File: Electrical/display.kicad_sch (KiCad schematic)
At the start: 22 parts, among them J4 Conn_02x04_Top_Bottom, U11 JM-S05422A-001, U6 DA56-11CGKWA

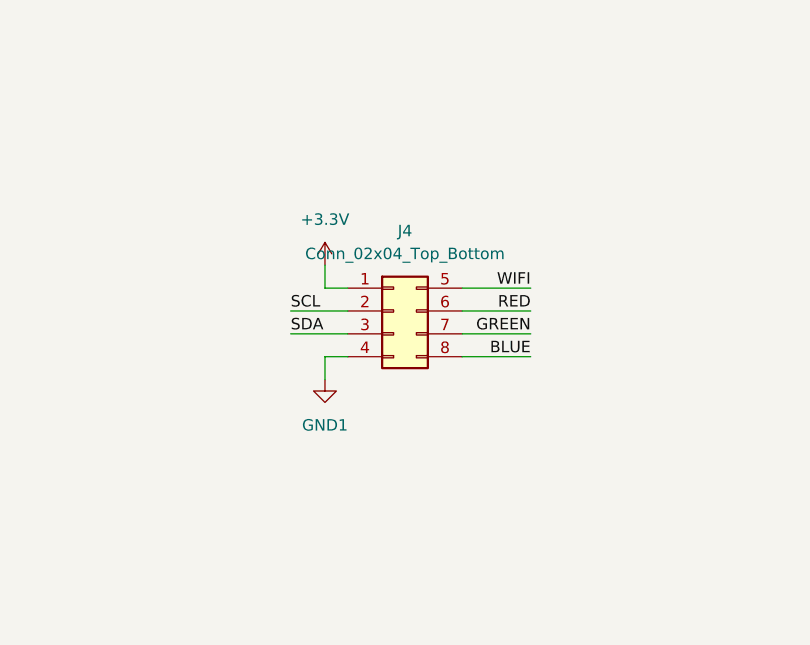
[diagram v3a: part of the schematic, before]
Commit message: Updated Display
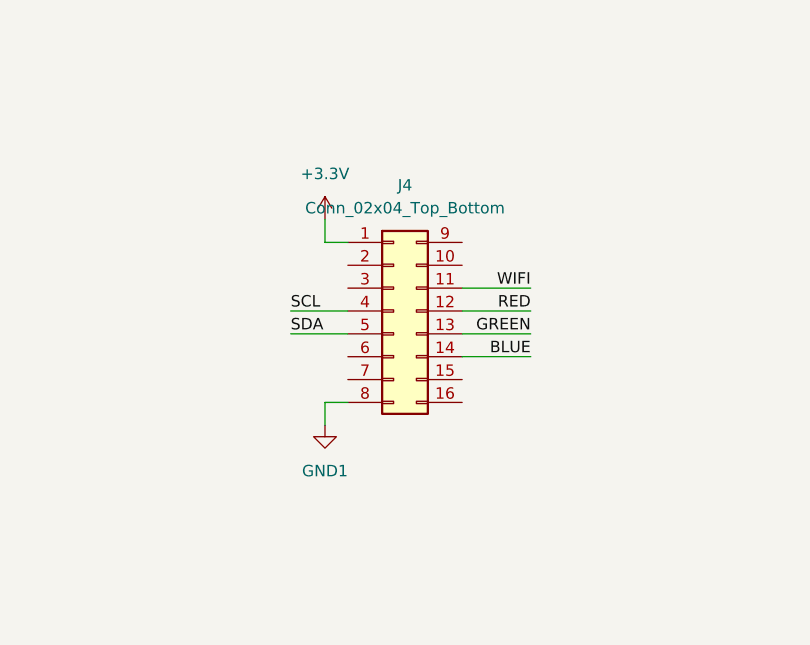
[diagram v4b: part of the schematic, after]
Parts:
- J4: footprint Connector_IDC:IDC-Header_2x04_P2.54mm_Vertical -> Connector_IDC:IDC-Header_2x08_P2.54mm_Vertical; symbol Connector_Generic:Conn_02x04_Top_Bottom -> Connector_Generic:Conn_02x08_Top_Bottom
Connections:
- net BLUE: now also J4.14 (Pin_14); no longer J4.8 (Pin_8)
- net GND1: now also J4.8 (Pin_8); no longer J4.4 (Pin_4)
- net GREEN: now also J4.13 (Pin_13); no longer J4.7 (Pin_7)
- net RED: now also J4.12 (Pin_12); no longer J4.6 (Pin_6)
- net SCL: now also J4.4 (Pin_4); no longer J4.2 (Pin_2)
- net SDA: now also J4.5 (Pin_5); no longer J4.3 (Pin_3)
- net WIFI: now also J4.11 (Pin_11); no longer J4.5 (Pin_5)
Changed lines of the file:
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@@
+    (stroke (width 0) (type default))
+  )
+  (wire (pts (xy 251.46 87.63) (xy 254 87.63))
     (stroke (width 0) (type default))
   )
@@
     (stroke (width 0) (type default))
   )
-  (wire (pts (xy 254 100.33) (xy 251.46 100.33))
+  (wire (pts (xy 251.46 85.09) (xy 251.46 87.63))
     (stroke (width 0) (type default))
   )
@@
     (stroke (width 0) (type default))
   )
-  (wire (pts (xy 251.46 100.33) (xy 251.46 102.87))
+  (wire (pts (xy 251.46 105.41) (xy 251.46 107.95))
     (stroke (width 0) (type default))
   )
@@
     (stroke (width 0) (type default))
   )
+  (wire (pts (xy 254 105.41) (xy 251.46 105.41))
+    (stroke (width 0) (type default))
+  )
   (wire (pts (xy 328.93 184.15) (xy 256.54 184.15))
     (stroke (width 0) (type default))
@@
     (stroke (width 0) (type default))
   )
-  (wire (pts (xy 251.46 90.17) (xy 251.46 92.71))
-    (stroke (width 0) (type default))
-  )
   (wire (pts (xy 140.97 20.32) (xy 140.97 85.09))
     (stroke (width 0) (type default))
@@
   )
   (wire (pts (xy 323.85 167.64) (xy 321.31 167.64))
-    (stroke (width 0) (type default))
-  )
-  (wire (pts (xy 251.46 92.71) (xy 254 92.71))
     (stroke (width 0) (type default))
   )
@@
     )
   )
-  (symbol (lib_id "power:GND1") (at 251.46 102.87 0) (unit 1)
-    (in_bom yes) (on_board yes) (dnp no) (fields_autoplaced)
-    (property "Reference" "#PWR024" (at 251.46 109.22 0)
-      (effects (font (size 1.27 1.27)) hide)
-    )
-    (property "Value" "GND1" (at 251.46 107.95 0)
-      (effects (font (size 1.27 1.27)))
-    )
-    (property "Footprint" "" (at 251.46 102.87 0)
-      (effects (font (size 1.27 1.27)) hide)
-    )
-    (property "Datasheet" "" (at 251.46 102.87 0)
-      (effects (font (size 1.27 1.27)) hide)
-    )
-    (pin "1")
-    (instances
-      (project "NMEA-2000-influxdb"
-        (path "/efe7a42c-525a-4afc-8476-4cc785240ca6/f595a6b6-5945-4ca8-806c-a50feeda2cc9"
-          (reference "#PWR024") (unit 1)
-        )
-      )
-    )
-  )
   (symbol (lib_id "power:+3.3V") (at 346.71 30.48 0) (unit 1)
     (in_bom yes) (on_board yes) (dnp no) (fields_autoplaced)
@@
     )
   )
+  (symbol (lib_id "power:+3.3V") (at 251.46 85.09 0) (unit 1)
+    (in_bom yes) (on_board yes) (dnp no) (fields_autoplaced)
+    (property "Reference" "#PWR023" (at 251.46 88.9 0)
+      (effects (font (size 1.27 1.27)) hide)
+    )
+    (property "Value" "+3.3V" (at 251.46 80.01 0)
+      (effects (font (size 1.27 1.27)))
+    )
+    (property "Footprint" "" (at 251.46 85.09 0)
+      (effects (font (size 1.27 1.27)) hide)
+    )
+    (property "Datasheet" "" (at 251.46 85.09 0)
+      (effects (font (size 1.27 1.27)) hide)
+    )
+    (pin "1")
+    (instances
+      (project "NMEA-2000-influxdb"
+        (path "/efe7a42c-525a-4afc-8476-4cc785240ca6/f595a6b6-5945-4ca8-806c-a50feeda2cc9"
+          (reference "#PWR023") (unit 1)
+        )
+      )
+    )
+  )
   (symbol (lib_id "Device:R") (at 270.51 212.09 90) (mirror x) (unit 1)
     (in_bom yes) (on_board yes) (dnp no)
@@
     )
   )
-  (symbol (lib_id "power:+3.3V") (at 251.46 90.17 0) (unit 1)
-    (in_bom yes) (on_board yes) (dnp no) (fields_autoplaced)
-    (property "Reference" "#PWR023" (at 251.46 93.98 0)
-      (effects (font (size 1.27 1.27)) hide)
-    )
-    (property "Value" "+3.3V" (at 251.46 85.09 0)
-      (effects (font (size 1.27 1.27)))
-    )
-    (property "Footprint" "" (at 251.46 90.17 0)
-      (effects (font (size 1.27 1.27)) hide)
-    )
-    (property "Datasheet" "" (at 251.46 90.17 0)
-      (effects (font (size 1.27 1.27)) hide)
-    )
-    (pin "1")
-    (instances
-      (project "NMEA-2000-influxdb"
-        (path "/efe7a42c-525a-4afc-8476-4cc785240ca6/f595a6b6-5945-4ca8-806c-a50feeda2cc9"
-          (reference "#PWR023") (unit 1)
+  (symbol (lib_id "power:GND1") (at 251.46 107.95 0) (unit 1)
+    (in_bom yes) (on_board yes) (dnp no) (fields_autoplaced)
+    (property "Reference" "#PWR024" (at 251.46 114.3 0)
+      (effects (font (size 1.27 1.27)) hide)
+    )
+    (property "Value" "GND1" (at 251.46 113.03 0)
+      (effects (font (size 1.27 1.27)))
+    )
+    (property "Footprint" "" (at 251.46 107.95 0)
+      (effects (font (size 1.27 1.27)) hide)
+    )
+    (property "Datasheet" "" (at 251.46 107.95 0)
+      (effects (font (size 1.27 1.27)) hide)
+    )
+    (pin "1")
+    (instances
+      (project "NMEA-2000-influxdb"
+        (path "/efe7a42c-525a-4afc-8476-4cc785240ca6/f595a6b6-5945-4ca8-806c-a50feeda2cc9"
+          (reference "#PWR024") (unit 1)
         )
       )
@@
     )
   )
-  (symbol (lib_id "Connector_Generic:Conn_02x04_Top_Bottom") (at 259.08 95.25 0) (unit 1)
-    (in_bom yes) (on_board yes) (dnp no) (fields_autoplaced)
-    (property "Reference" "J4" (at 260.35 86.36 0)
-      (effects (font (size 1.27 1.27)))
-    )
-    (property "Value" "Conn_02x04_Top_Bottom" (at 260.35 88.9 0)
-      (effects (font (size 1.27 1.27)))
-    )
-    (property "Footprint" "Connector_IDC:IDC-Header_2x04_P2.54mm_Vertical" (at 259.08 95.25 0)
+  (symbol (lib_id "Connector_Generic:Conn_02x08_Top_Bottom") (at 259.08 95.25 0) (unit 1)
+    (in_bom yes) (on_board yes) (dnp no) (fields_autoplaced)
+    (property "Reference" "J4" (at 260.35 81.28 0)
+      (effects (font (size 1.27 1.27)))
+    )
+    (property "Value" "Conn_02x04_Top_Bottom" (at 260.35 83.82 0)
+      (effects (font (size 1.27 1.27)))
+    )
+    (property "Footprint" "Connector_IDC:IDC-Header_2x08_P2.54mm_Vertical" (at 259.08 95.25 0)
       (effects (font (size 1.27 1.27)) hide)
     )
@@
     (pin "1")
     (pin "8")
-    (instances
-      (project "NMEA-2000-influxdb"
+    (pin "12")
+    (pin "16")
+    (pin "15")
+    (pin "14")
+    (pin "11")
+    (pin "10")
+    (pin "13")
+    (pin "9")
+    (instances
+      (project "NMEA-2000-influxdb"

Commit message: Updated schematic
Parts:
- added D2, D3, D4: LED, LED_THT:LED_D5.0mm, symbol Device:LED
- added J5: Conn_01x04, TerminalBlock_Phoenix:TerminalBlock_Phoenix_MKDS-1,5-4-5.08_1x04_P5.08mm_Horizontal, symbol Connector_Generic:Conn_01x04
- added JP1, JP3, JP4, JP5, JP6, JP7, JP9: Jumper_2_Bridged, Connector_PinHeader_2.54mm:PinHeader_1x02_P2.54mm_Vertical, symbol Jumper:Jumper_2_Bridged
- added JP2, JP8: Jumper_2_Open, Connector_PinHeader_2.54mm:PinHeader_1x02_P2.54mm_Vertical, symbol Jumper:Jumper_2_Open
- added R17, R7: 38k, Resistor_THT:R_Axial_DIN0204_L3.6mm_D1.6mm_P5.08mm_Horizontal, symbol Device:R
- added R2, R3, R4: 220R, Resistor_THT:R_Axial_DIN0204_L3.6mm_D1.6mm_P5.08mm_Horizontal, symbol Device:R
- added SW1, SW2: SW_Push, Button_Switch_THT:SW_PUSH_6mm_H13mm, symbol Switch:SW_Push
- D5: renamed from D2; value LED_ABGR -> TJ-L5FYTXHTCYLCRGB-A5
- J4: value Conn_02x04_Top_Bottom -> Conn_02x04
- R1: renamed from R12; value R -> 220R
- renumbered R9 to R10, R10 to R11, R3 to R12, R5 to R13, R11 to R14, R4 to R15, R6 to R16, R7 to R18, R13 to R5, R1 to R6, R2 to R8, R8 to R9, U11 to U8, U6 to U9
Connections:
- net +3.3V: now also J4.2 (Pin_2), R2.1, R3.1, R4.1, SW1.1, SW2.1; no longer J4.1 (Pin_1)
- net +5VD: now also J4.1 (Pin_1), J5.1 (Pin_1)
- net BLUE: now also J4.15 (Pin_15); no longer J4.14 (Pin_14)
- net GND1: now also J4.16 (Pin_16); no longer J4.8 (Pin_8)
- net GREEN: now also J4.14 (Pin_14); no longer J4.13 (Pin_13)
- net RED: now also J4.13 (Pin_13); no longer J4.12 (Pin_12)
- net SCL: now also J4.5 (Pin_5); no longer J4.4 (Pin_4)
- net SDA: now also J4.6 (Pin_6); no longer J4.5 (Pin_5)
- net at U1.23 (ROW2/A0), U8.4 (M): now also JP5.2 (B); no longer R13.2
- net at U1.24 (ROW1/A1), U8.2 (N): now also JP7.2 (B); no longer R16.2
- net at U1.25 (ROW0/A2), U8.1 (E): now also JP9.2 (B); no longer R18.2
- net at R6.1, R8.1, U1.2 (COM0/AD): now also R7.1
- net at U1.23 (ROW2/A0), U6.12 (DIG2_F): now also JP3.2 (B); no longer R8.2
- net at R12.1, R15.1, U1.2 (COM0/AD): now also R17.1
- net at U1.23 (ROW2/A0), U9.12 (DIG2_F): now also JP8.2 (B)
- net at U1.24 (ROW1/A1), U9.7 (DIG2_G): now also JP6.2 (B); no longer R15.2
- net at U1.25 (ROW0/A2), U9.9 (DP2): now also JP4.2 (B); no longer R12.2
- net at U1.25 (ROW0/A2), U6.9 (DP2): now also JP1.2 (B); no longer R6.2
- net at U1.24 (ROW1/A1), U6.7 (DIG2_G): now also JP2.2 (B)
- net SD_ST: now reaches J4.10 (Pin_10)
- net SD_ST: now also D2.1 (K)
- net CAN_H: now reaches J4.3 (Pin_3)
- net CAN_H: now also J5.2 (Pin_2)
- net SW_TG: now reaches J4.7 (Pin_7)
- net SW_TG: now also SW1.2
- net CAN_ST: now reaches J4.9 (Pin_9)
- net CAN_ST: now also D1.1 (K)
- net WIFI renamed RTC_ST
- net RTC_ST: now also D3.1 (K); no longer D1.1 (K)
- new net: D3.2 (A), R3.2
- new net: JP2.1 (A), R7.2
- new net: JP5.1 (A), R13.2
- new net: JP7.1 (A), R16.2
- new net: JP6.1 (A), R15.2
- new net: JP3.1 (A), R8.2
- new net: JP1.1 (A), R6.2
- new net: JP9.1 (A), R18.2
- new net: D4.2 (A), R4.2
- new net: JP8.1 (A), R17.2
- new net: JP4.1 (A), R12.2
- new net: D2.2 (A), R2.2
- new net CAN_L: J4.4 (Pin_4), J5.3 (Pin_3)
- new net GND: J5.4 (Pin_4)
- new net SW_CY: J4.8 (Pin_8), SW2.2
- new net WIFI_ST: D4.1 (K), J4.12 (Pin_12)
- no-connect marks 21 -> 17
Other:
- moved on the sheet: D1, J4, R1, R10, R11, R14, R9, U8

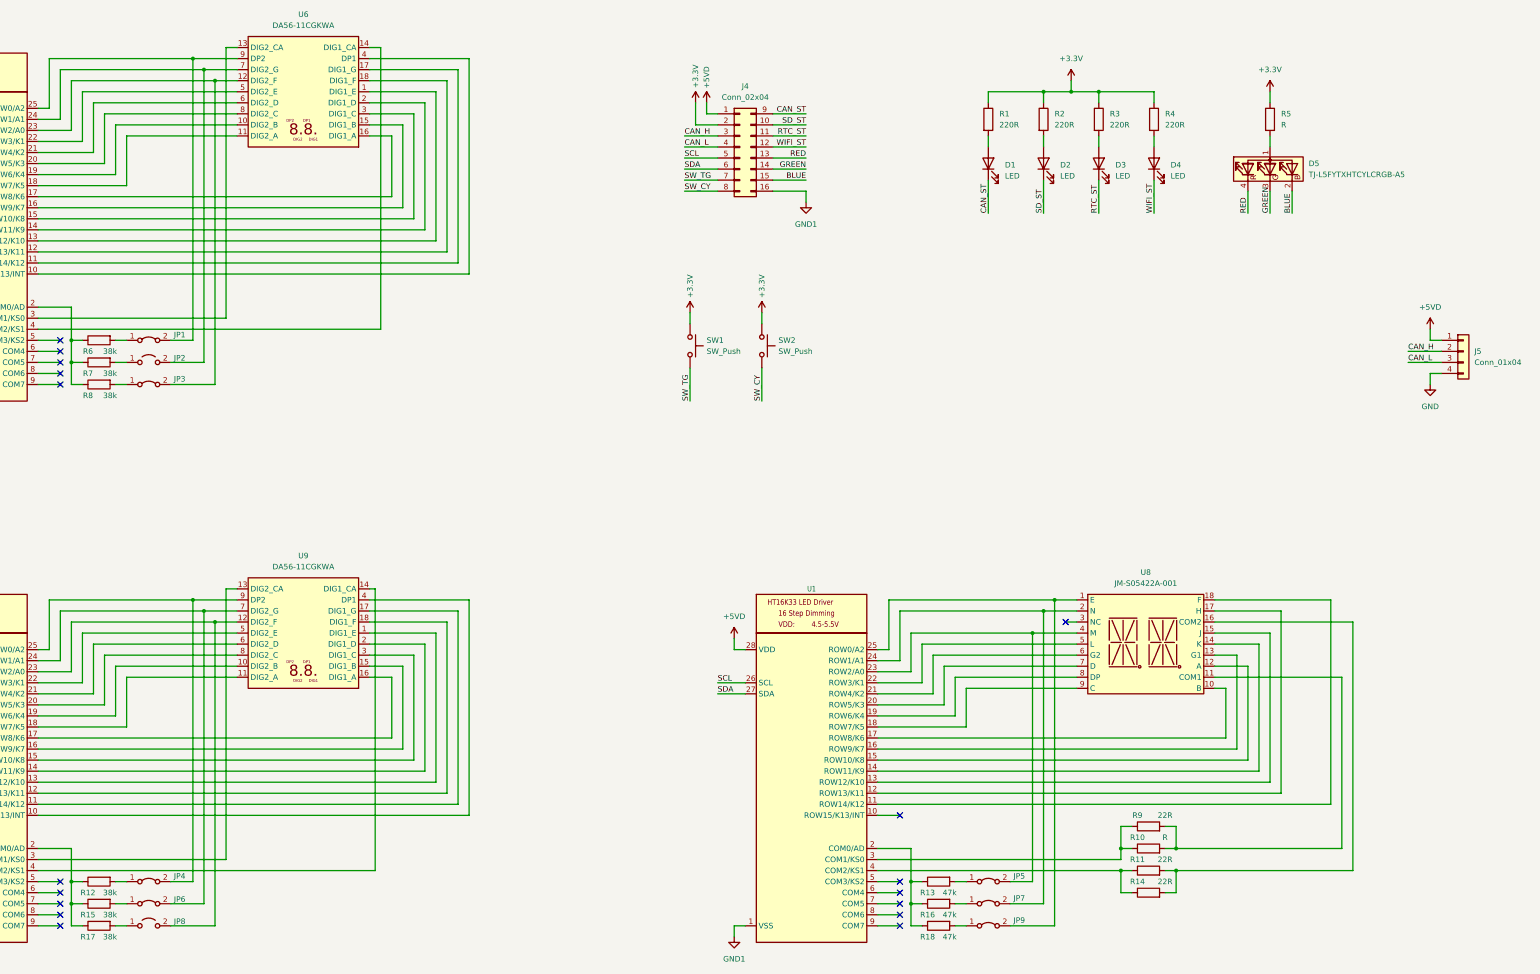
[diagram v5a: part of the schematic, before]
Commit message: Added Backup CAN Transceiver Module Switched Push Button for SPST Switch Added Heatsink for LM7805
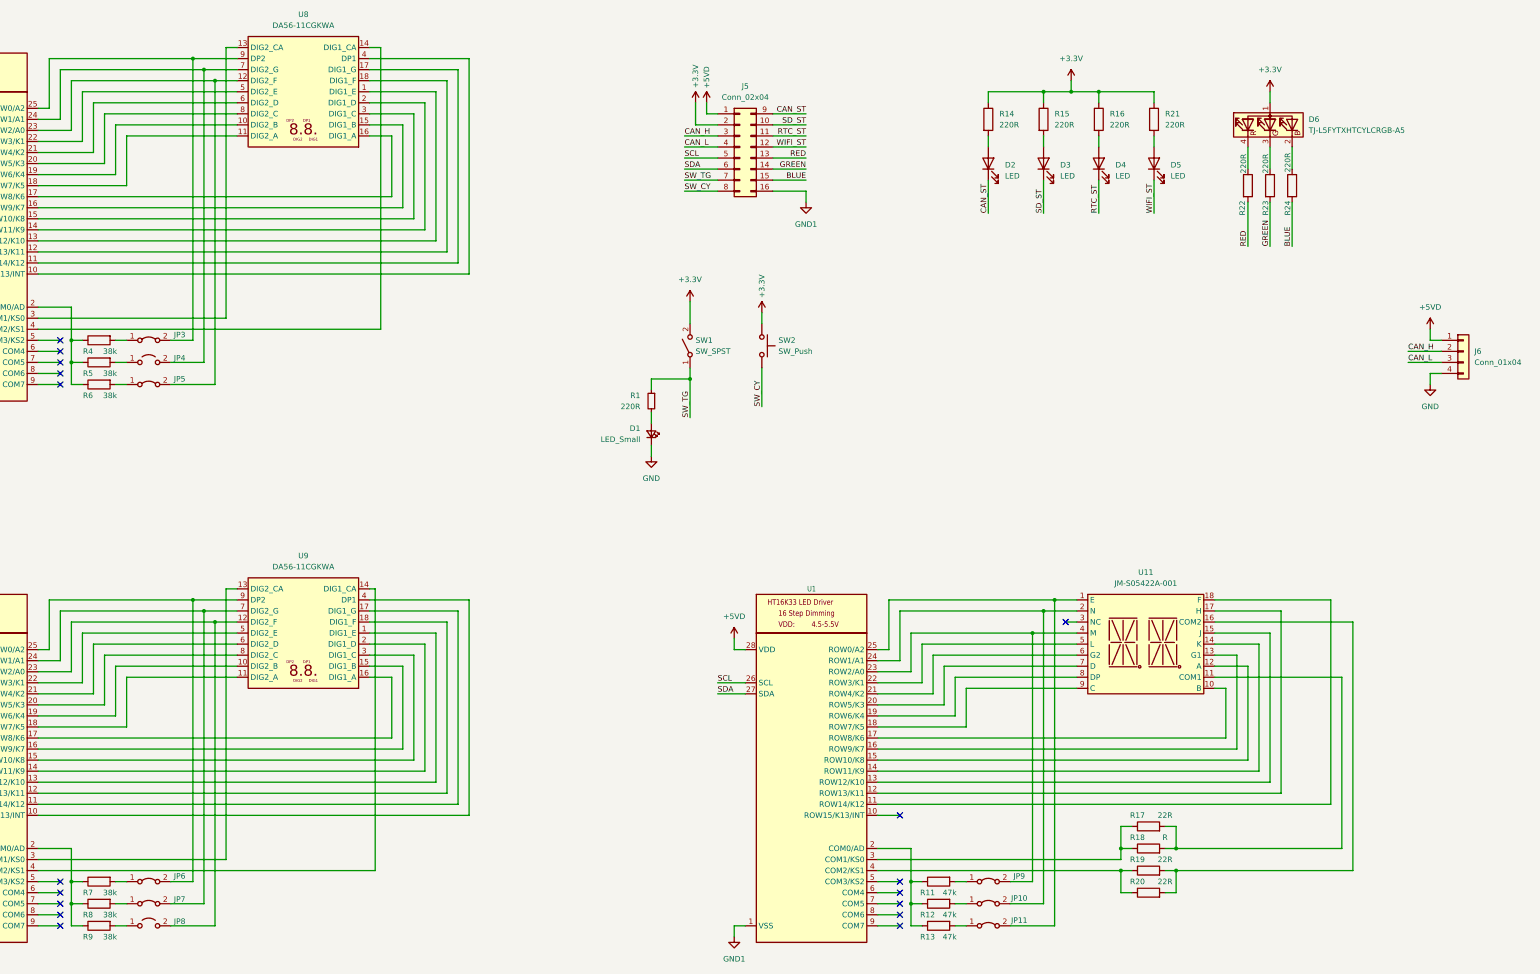
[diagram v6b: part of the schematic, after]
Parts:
- removed R5: R, Resistor_THT:R_Axial_DIN0204_L3.6mm_D1.6mm_P5.08mm_Horizontal, symbol Device:R
- removed SW1: SW_Push, Button_Switch_THT:SW_PUSH_6mm_H13mm, symbol Switch:SW_Push
- added D1: LED_Small, Connector_PinSocket_2.54mm:PinSocket_1x04_P2.54mm_Horizontal, symbol Device:LED_Small
- added R1: 220R, Resistor_THT:R_Axial_DIN0204_L3.6mm_D1.6mm_P5.08mm_Horizontal, symbol Device:R_Small
- added R22, R23, R24: 220R, Resistor_THT:R_Axial_DIN0204_L3.6mm_D1.6mm_P5.08mm_Horizontal, symbol Device:R
- added SW1: SW_SPST, symbol Switch:SW_SPST
- renumbered D1 to D2, D2 to D3, D3 to D4, D4 to D5, D5 to D6, J4 to J5, J5 to J6, JP7 to JP10, JP9 to JP11, JP1 to JP3, JP2 to JP4, JP3 to JP5, JP4 to JP6, JP6 to JP7, JP5 to JP9, R13 to R11, R16 to R12, R18 to R13, R1 to R14, R2 to R15, R3 to R16, R9 to R17, R10 to R18, R11 to R19, R14 to R20, R4 to R21, R6 to R4, R7 to R5, R8 to R6, R12 to R7, R15 to R8, R17 to R9, U8 to U11, U6 to U8
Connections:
- net +3.3V: now also D6.1 (A), SW1.2 (B)
- net BLUE: now also R24.2; no longer D6.2 (BK)
- net GND: now also D1.1 (K)
- net GREEN: now also R23.2; no longer D6.3 (GK)
- net RED: now also R22.2; no longer D6.4 (RK)
- net SW_TG: now also R1.1, SW1.1 (A)
- new net: D6.4 (RK), R22.1
- new net: D6.3 (GK), R23.1
- new net: D6.2 (BK), R24.1
- new net: D1.2 (A), R1.2
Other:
- moved on the sheet: D6
